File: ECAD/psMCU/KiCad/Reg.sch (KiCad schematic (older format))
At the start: 17 parts, among them U258 SN74LVC1G04DCK, U259 CD74HC173PW, U260 CD74HC173PW, U261 SN74LVC1G126DCK, U262 SN74LVC1G04DCK, U263 SN74HC245PW

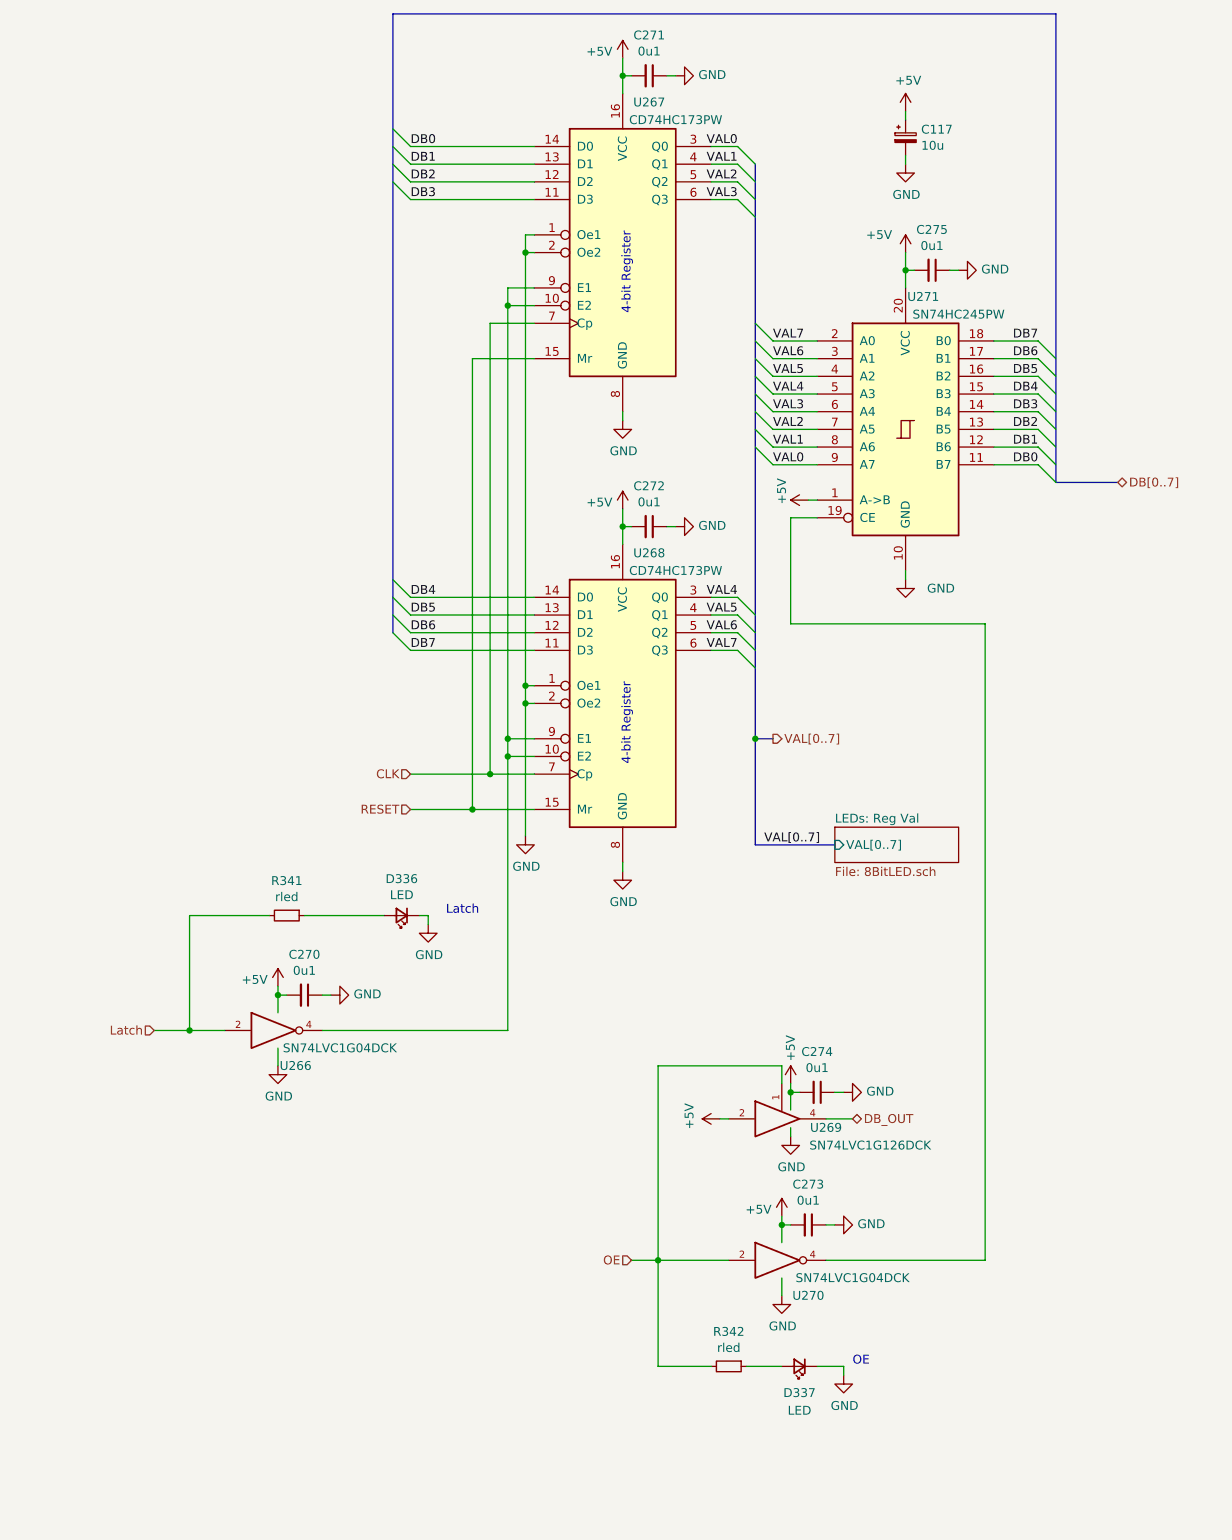
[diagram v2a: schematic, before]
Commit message: Sch: Improved Clk/Reset distribution, moved to global labels
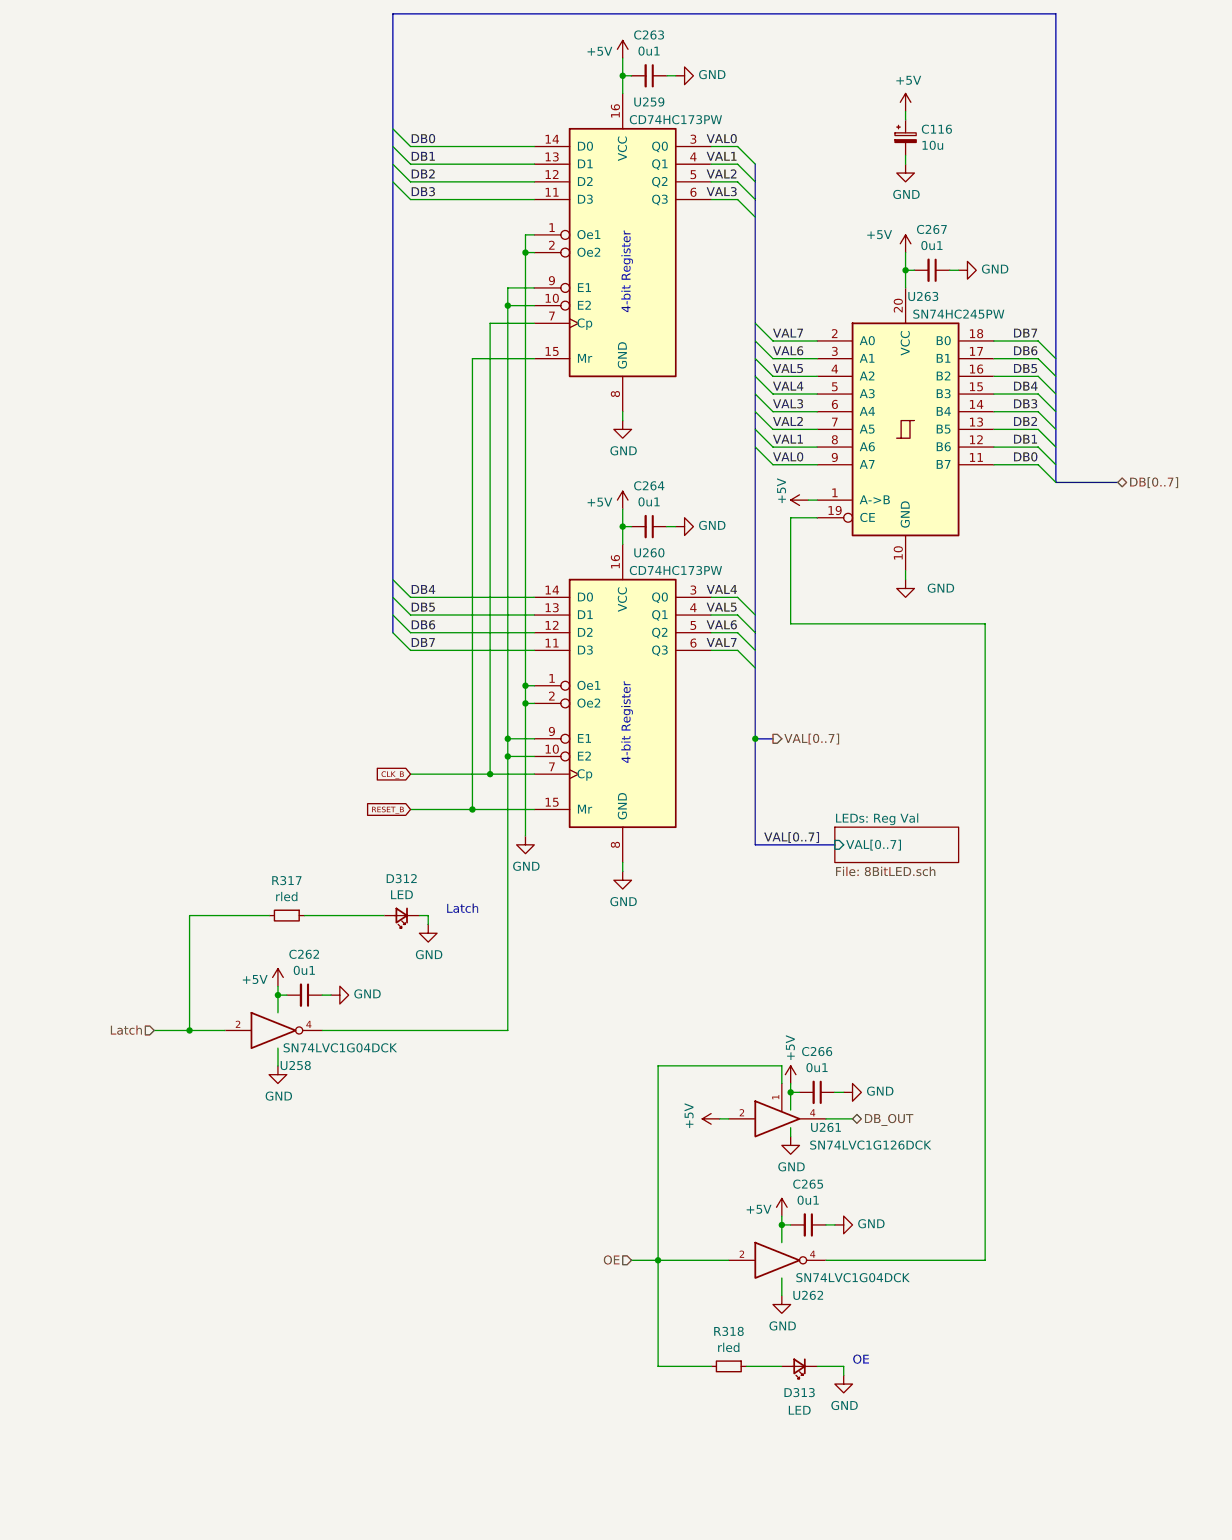
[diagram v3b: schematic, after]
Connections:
- net CLK renamed CLK_B
- net RESET renamed RESET_B
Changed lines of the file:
@@
 $Descr A4 8268 11693 portrait
 encoding utf-8
-Sheet 60 96
+Sheet 56 97
 Title "psMCU"
 Date "2022-02-13"
@@
 AR Path="/61C3CF7F/5F0B921F" Ref="U262"  Part="1"
 AR Path="/61C3CF88/5F0B921F" Ref="U270"  Part="1"
-F 0 "U270" H 4950 7900 50  0000 C CNN
+F 0 "U262" H 4950 7900 50  0000 C CNN
 F 1 "SN74LVC1G04DCK" H 5200 8000 50  0000 C CNN
 F 2 "Package_TO_SOT_SMD:SOT-353_SC-70-5" H 4800 8100 50  0001 C CNN
@@
 AR Path="/61C3CF7F/5F0B922C" Ref="C265"  Part="1"
 AR Path="/61C3CF88/5F0B922C" Ref="C273"  Part="1"
-F 0 "C273" V 4721 7900 50  0000 C CNN
+F 0 "C265" V 4721 7900 50  0000 C CNN
 F 1 "0u1" V 4812 7900 50  0000 C CNN
 F 2 "NoRef_Footprints:C_0603_1608Metric_NoRef" H 4950 7900 50  0001 C CNN
@@
 AR Path="/61C3CF7F/5EF8C8C3" Ref="C262"  Part="1"
 AR Path="/61C3CF88/5EF8C8C3" Ref="C270"  Part="1"
-F 0 "C270" V 1871 6600 50  0000 C CNN
+F 0 "C262" V 1871 6600 50  0000 C CNN
 F 1 "0u1" V 1962 6600 50  0000 C CNN
 F 2 "NoRef_Footprints:C_0603_1608Metric_NoRef" H 2100 6600 50  0001 C CNN
@@
 AR Path="/61C3CF7F/5EF829AC" Ref="U258"  Part="1"
 AR Path="/61C3CF88/5EF829AC" Ref="U266"  Part="1"
-F 0 "U266" H 2050 6600 50  0000 C CNN
+F 0 "U258" H 2050 6600 50  0000 C CNN
 F 1 "SN74LVC1G04DCK" H 2300 6700 50  0000 C CNN
 F 2 "Package_TO_SOT_SMD:SOT-353_SC-70-5" H 1950 6800 50  0001 C CNN
@@
 AR Path="/61C3CF7F/5ED710F5" Ref="C267"  Part="1"
 AR Path="/61C3CF88/5ED710F5" Ref="C275"  Part="1"
-F 0 "C275" V 5421 2500 50  0000 C CNN
+F 0 "C267" V 5421 2500 50  0000 C CNN
 F 1 "0u1" V 5512 2500 50  0000 C CNN
 F 2 "NoRef_Footprints:C_0603_1608Metric_NoRef" H 5650 2500 50  0001 C CNN
@@
 AR Path="/61C3CF7F/5ED4E5FA" Ref="U263"  Part="1"
 AR Path="/61C3CF88/5ED4E5FA" Ref="U271"  Part="1"
-F 0 "U271" H 5600 4150 50  0000 C CNN
+F 0 "U263" H 5600 4150 50  0000 C CNN
 F 1 "SN74HC245PW" H 5800 4050 50  0000 C CNN
 F 2 "Package_SO:TSSOP-20_4.4x6.5mm_P0.65mm" H 5500 3400 50  0001 C CNN
@@
 AR Path="/61C3CF7F/5ED33B48" Ref="C264"  Part="1"
 AR Path="/61C3CF88/5ED33B48" Ref="C272"  Part="1"
-F 0 "C272" V 3821 3950 50  0000 C CNN
+F 0 "C264" V 3821 3950 50  0000 C CNN
 F 1 "0u1" V 3912 3950 50  0000 C CNN
 F 2 "NoRef_Footprints:C_0603_1608Metric_NoRef" H 4050 3950 50  0001 C CNN
@@
 AR Path="/61C3CF7F/5ED33B3B" Ref="U260"  Part="1"
 AR Path="/61C3CF88/5ED33B3B" Ref="U268"  Part="1"
-F 0 "U268" H 4050 5800 50  0000 C CNN
+F 0 "U260" H 4050 5800 50  0000 C CNN
 F 1 "CD74HC173PW" H 4200 5700 50  0000 C CNN
 F 2 "Package_SO:TSSOP-16_4.4x5mm_P0.65mm" H 3900 4950 50  0001 C CNN
@@
 AR Path="/61C3CF7F/5ED2F1C3" Ref="C263"  Part="1"
 AR Path="/61C3CF88/5ED2F1C3" Ref="C271"  Part="1"
-F 0 "C271" V 3821 1400 50  0000 C CNN
+F 0 "C263" V 3821 1400 50  0000 C CNN
 F 1 "0u1" V 3912 1400 50  0000 C CNN
 F 2 "NoRef_Footprints:C_0603_1608Metric_NoRef" H 4050 1400 50  0001 C CNN
@@
 AR Path="/61C3CF7F/5ED2BCE4" Ref="U259"  Part="1"
 AR Path="/61C3CF88/5ED2BCE4" Ref="U267"  Part="1"
-F 0 "U267" H 4050 3250 50  0000 C CNN
+F 0 "U259" H 4050 3250 50  0000 C CNN
 F 1 "CD74HC173PW" H 4200 3150 50  0000 C CNN
 F 2 "Package_SO:TSSOP-16_4.4x5mm_P0.65mm" H 3900 2400 50  0001 C CNN
@@
 Text HLabel 4750 5150 2    50   Output ~ 0
 VAL[0..7]
-Text HLabel 2700 5550 0    50   Input ~ 0
-RESET
-Text HLabel 2700 5350 0    50   Input ~ 0
-CLK
 Wire Bus Line
 	4750 5150 4650 5150
@@
 AR Path="/61C3CF7F/5F369738" Ref="C266"  Part="1"
 AR Path="/61C3CF88/5F369738" Ref="C274"  Part="1"
-F 0 "C274" V 4771 7150 50  0000 C CNN
+F 0 "C266" V 4771 7150 50  0000 C CNN
 F 1 "0u1" V 4862 7150 50  0000 C CNN
 F 2 "NoRef_Footprints:C_0603_1608Metric_NoRef" H 5000 7150 50  0001 C CNN
@@
 AR Path="/61C3CF7F/62B8F34C" Ref="D313"  Part="1"
 AR Path="/61C3CF88/62B8F34C" Ref="D337"  Part="1"
-F 0 "D337" H 4900 8850 50  0000 C CNN
+F 0 "D313" H 4900 8850 50  0000 C CNN
 F 1 "LED" H 4900 8950 50  0000 C CNN
 F 2 "NoRef_Footprints:D_0603_1608Metric_NoRef" V 4900 8700 50  0001 C CNN
@@
 AR Path="/61C3CF7F/62B8F35A" Ref="R318"  Part="1"
 AR Path="/61C3CF88/62B8F35A" Ref="R342"  Part="1"
-F 0 "R342" V 4304 8700 50  0000 C CNN
+F 0 "R318" V 4304 8700 50  0000 C CNN
 F 1 "rled" V 4395 8700 50  0000 C CNN
 F 2 "NoRef_Footprints:R_0603_1608Metric_NoRef" H 4500 8700 50  0001 C CNN
@@
 AR Path="/61C3CF7F/62B948BD" Ref="D312"  Part="1"
 AR Path="/61C3CF88/62B948BD" Ref="D336"  Part="1"
-F 0 "D336" H 2650 5943 50  0000 C CNN
+F 0 "D312" H 2650 5943 50  0000 C CNN
 F 1 "LED" H 2650 6034 50  0000 C CNN
 F 2 "NoRef_Footprints:D_0603_1608Metric_NoRef" V 2650 6150 50  0001 C CNN
@@
 AR Path="/61C3CF7F/62B948CB" Ref="R317"  Part="1"
 AR Path="/61C3CF88/62B948CB" Ref="R341"  Part="1"
-F 0 "R341" V 1804 6150 50  0000 C CNN
+F 0 "R317" V 1804 6150 50  0000 C CNN
 F 1 "rled" V 1895 6150 50  0000 C CNN
 F 2 "NoRef_Footprints:R_0603_1608Metric_NoRef" H 2000 6150 50  0001 C CNN
@@
 AR Path="/61C3CF7F/5F369721" Ref="U261"  Part="1"
 AR Path="/61C3CF88/5F369721" Ref="U269"  Part="1"
-F 0 "U269" H 5050 7250 50  0000 C CNN
+F 0 "U261" H 5050 7250 50  0000 C CNN
 F 1 "SN74LVC1G126DCK" H 5300 7150 50  0000 C CNN
 F 2 "Package_TO_SOT_SMD:SOT-353_SC-70-5" H 4800 7300 50  0001 C CNN
@@
 AR Path="/61C3CF88/6244A237" Ref="C117"  Part="1"
 AR Path="/61C3CF7F/6244A237" Ref="C116"  Part="1"
-F 0 "C117" H 5588 1796 50  0000 L CNN
+F 0 "C116" H 5588 1796 50  0000 L CNN
 F 1 "10u" H 5588 1705 50  0000 L CNN
 F 2 "" H 5500 1750 50  0001 C CNN
@@
 	1    0    0    -1
 $EndComp
+Text GLabel 2700 5350 0    31   Input ~ 0
+CLK_B
+Text GLabel 2700 5550 0    31   Input ~ 0
+RESET_B
 Wire Bus Line
 	2600 1050 2600 4550

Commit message: Sch: Implemented new Statemachine
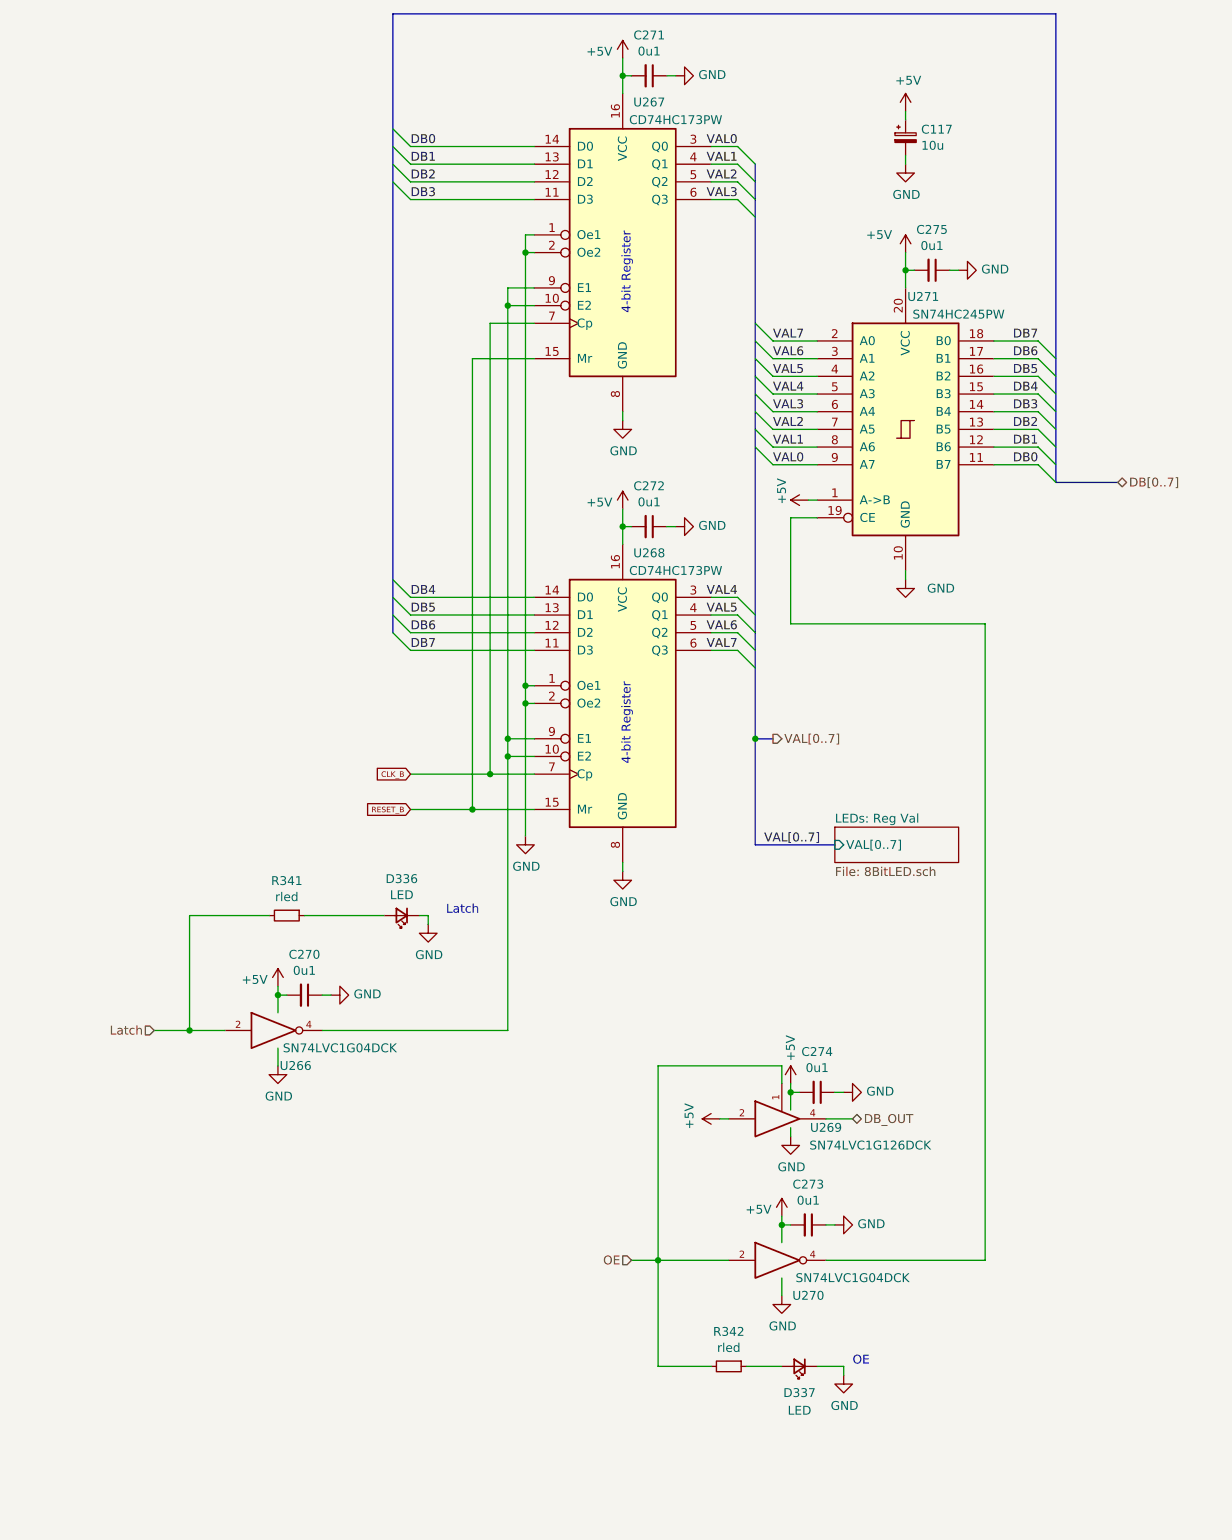
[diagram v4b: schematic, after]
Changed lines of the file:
@@
 $Descr A4 8268 11693 portrait
 encoding utf-8
-Sheet 56 97
+Sheet 56 102
 Title "psMCU"
 Date "2022-02-13"
@@
 AR Path="/61C3CF7F/5F0B921F" Ref="U262"  Part="1"
 AR Path="/61C3CF88/5F0B921F" Ref="U270"  Part="1"
-F 0 "U262" H 4950 7900 50  0000 C CNN
+F 0 "U270" H 4950 7900 50  0000 C CNN
 F 1 "SN74LVC1G04DCK" H 5200 8000 50  0000 C CNN
 F 2 "Package_TO_SOT_SMD:SOT-353_SC-70-5" H 4800 8100 50  0001 C CNN
@@
 AR Path="/61C3CF7F/5F0B922C" Ref="C265"  Part="1"
 AR Path="/61C3CF88/5F0B922C" Ref="C273"  Part="1"
-F 0 "C265" V 4721 7900 50  0000 C CNN
+F 0 "C273" V 4721 7900 50  0000 C CNN
 F 1 "0u1" V 4812 7900 50  0000 C CNN
 F 2 "NoRef_Footprints:C_0603_1608Metric_NoRef" H 4950 7900 50  0001 C CNN
@@
 AR Path="/61C3CF7F/5EF8C8C3" Ref="C262"  Part="1"
 AR Path="/61C3CF88/5EF8C8C3" Ref="C270"  Part="1"
-F 0 "C262" V 1871 6600 50  0000 C CNN
+F 0 "C270" V 1871 6600 50  0000 C CNN
 F 1 "0u1" V 1962 6600 50  0000 C CNN
 F 2 "NoRef_Footprints:C_0603_1608Metric_NoRef" H 2100 6600 50  0001 C CNN
@@
 AR Path="/61C3CF7F/5EF829AC" Ref="U258"  Part="1"
 AR Path="/61C3CF88/5EF829AC" Ref="U266"  Part="1"
-F 0 "U258" H 2050 6600 50  0000 C CNN
+F 0 "U266" H 2050 6600 50  0000 C CNN
 F 1 "SN74LVC1G04DCK" H 2300 6700 50  0000 C CNN
 F 2 "Package_TO_SOT_SMD:SOT-353_SC-70-5" H 1950 6800 50  0001 C CNN
@@
 AR Path="/61C3CF7F/5ED710F5" Ref="C267"  Part="1"
 AR Path="/61C3CF88/5ED710F5" Ref="C275"  Part="1"
-F 0 "C267" V 5421 2500 50  0000 C CNN
+F 0 "C275" V 5421 2500 50  0000 C CNN
 F 1 "0u1" V 5512 2500 50  0000 C CNN
 F 2 "NoRef_Footprints:C_0603_1608Metric_NoRef" H 5650 2500 50  0001 C CNN
@@
 AR Path="/61C3CF7F/5ED4E5FA" Ref="U263"  Part="1"
 AR Path="/61C3CF88/5ED4E5FA" Ref="U271"  Part="1"
-F 0 "U263" H 5600 4150 50  0000 C CNN
+F 0 "U271" H 5600 4150 50  0000 C CNN
 F 1 "SN74HC245PW" H 5800 4050 50  0000 C CNN
 F 2 "Package_SO:TSSOP-20_4.4x6.5mm_P0.65mm" H 5500 3400 50  0001 C CNN
@@
 AR Path="/61C3CF7F/5ED33B48" Ref="C264"  Part="1"
 AR Path="/61C3CF88/5ED33B48" Ref="C272"  Part="1"
-F 0 "C264" V 3821 3950 50  0000 C CNN
+F 0 "C272" V 3821 3950 50  0000 C CNN
 F 1 "0u1" V 3912 3950 50  0000 C CNN
 F 2 "NoRef_Footprints:C_0603_1608Metric_NoRef" H 4050 3950 50  0001 C CNN
@@
 AR Path="/61C3CF7F/5ED33B3B" Ref="U260"  Part="1"
 AR Path="/61C3CF88/5ED33B3B" Ref="U268"  Part="1"
-F 0 "U260" H 4050 5800 50  0000 C CNN
+F 0 "U268" H 4050 5800 50  0000 C CNN
 F 1 "CD74HC173PW" H 4200 5700 50  0000 C CNN
 F 2 "Package_SO:TSSOP-16_4.4x5mm_P0.65mm" H 3900 4950 50  0001 C CNN
@@
 AR Path="/61C3CF7F/5ED2F1C3" Ref="C263"  Part="1"
 AR Path="/61C3CF88/5ED2F1C3" Ref="C271"  Part="1"
-F 0 "C263" V 3821 1400 50  0000 C CNN
+F 0 "C271" V 3821 1400 50  0000 C CNN
 F 1 "0u1" V 3912 1400 50  0000 C CNN
 F 2 "NoRef_Footprints:C_0603_1608Metric_NoRef" H 4050 1400 50  0001 C CNN
@@
 AR Path="/61C3CF7F/5ED2BCE4" Ref="U259"  Part="1"
 AR Path="/61C3CF88/5ED2BCE4" Ref="U267"  Part="1"
-F 0 "U259" H 4050 3250 50  0000 C CNN
+F 0 "U267" H 4050 3250 50  0000 C CNN
 F 1 "CD74HC173PW" H 4200 3150 50  0000 C CNN
 F 2 "Package_SO:TSSOP-16_4.4x5mm_P0.65mm" H 3900 2400 50  0001 C CNN
@@
 AR Path="/61C3CF7F/5F369738" Ref="C266"  Part="1"
 AR Path="/61C3CF88/5F369738" Ref="C274"  Part="1"
-F 0 "C266" V 4771 7150 50  0000 C CNN
+F 0 "C274" V 4771 7150 50  0000 C CNN
 F 1 "0u1" V 4862 7150 50  0000 C CNN
 F 2 "NoRef_Footprints:C_0603_1608Metric_NoRef" H 5000 7150 50  0001 C CNN
@@
 AR Path="/61C3CF7F/62B8F34C" Ref="D313"  Part="1"
 AR Path="/61C3CF88/62B8F34C" Ref="D337"  Part="1"
-F 0 "D313" H 4900 8850 50  0000 C CNN
+F 0 "D337" H 4900 8850 50  0000 C CNN
 F 1 "LED" H 4900 8950 50  0000 C CNN
 F 2 "NoRef_Footprints:D_0603_1608Metric_NoRef" V 4900 8700 50  0001 C CNN
@@
 AR Path="/61C3CF7F/62B8F35A" Ref="R318"  Part="1"
 AR Path="/61C3CF88/62B8F35A" Ref="R342"  Part="1"
-F 0 "R318" V 4304 8700 50  0000 C CNN
+F 0 "R342" V 4304 8700 50  0000 C CNN
 F 1 "rled" V 4395 8700 50  0000 C CNN
 F 2 "NoRef_Footprints:R_0603_1608Metric_NoRef" H 4500 8700 50  0001 C CNN
@@
 AR Path="/61C3CF7F/62B948BD" Ref="D312"  Part="1"
 AR Path="/61C3CF88/62B948BD" Ref="D336"  Part="1"
-F 0 "D312" H 2650 5943 50  0000 C CNN
+F 0 "D336" H 2650 5943 50  0000 C CNN
 F 1 "LED" H 2650 6034 50  0000 C CNN
 F 2 "NoRef_Footprints:D_0603_1608Metric_NoRef" V 2650 6150 50  0001 C CNN
@@
 AR Path="/61C3CF7F/62B948CB" Ref="R317"  Part="1"
 AR Path="/61C3CF88/62B948CB" Ref="R341"  Part="1"
-F 0 "R317" V 1804 6150 50  0000 C CNN
+F 0 "R341" V 1804 6150 50  0000 C CNN
 F 1 "rled" V 1895 6150 50  0000 C CNN
 F 2 "NoRef_Footprints:R_0603_1608Metric_NoRef" H 2000 6150 50  0001 C CNN
@@
 AR Path="/61C3CF7F/5F369721" Ref="U261"  Part="1"
 AR Path="/61C3CF88/5F369721" Ref="U269"  Part="1"
-F 0 "U261" H 5050 7250 50  0000 C CNN
+F 0 "U269" H 5050 7250 50  0000 C CNN
 F 1 "SN74LVC1G126DCK" H 5300 7150 50  0000 C CNN
 F 2 "Package_TO_SOT_SMD:SOT-353_SC-70-5" H 4800 7300 50  0001 C CNN
@@
 AR Path="/61C3CF88/6244A237" Ref="C117"  Part="1"
 AR Path="/61C3CF7F/6244A237" Ref="C116"  Part="1"
-F 0 "C116" H 5588 1796 50  0000 L CNN
+F 0 "C117" H 5588 1796 50  0000 L CNN
 F 1 "10u" H 5588 1705 50  0000 L CNN
 F 2 "" H 5500 1750 50  0001 C CNN
